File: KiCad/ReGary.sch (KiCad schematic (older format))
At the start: 10 parts, among them U3 SN74CBTD16210, U4 SN74CBTD16210, U5 SN74CBTD16210, U6 SN74CBTD16210, U7 PLCC_84_plug, U8 PLCC_84_plug

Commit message: Add Fat Gary socket symbol and change to it
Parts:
- removed U7: PLCC_84_plug, ReGary:PLCC-84_Plug_P1.27mm_mirrored, symbol ReGary:Super_Buster_socket
- added U7: PLCC_84_plug, ReGary:PLCC-84_Plug_P1.27mm_mirrored, symbol ReGary:Fat_Gary_socket
- U8: symbol ReGary:Super_Buster_socket -> ReGary:Fat_Gary_socket
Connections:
- net +5V: no longer U8.42 (VCC), U8.84 (VCC)
- net A0: no longer U8.5 (A0)
- net A1: no longer U8.4 (A1)
- net A2: no longer U8.3 (A2)
- net A3: no longer U8.48 (A3)
- net ABOE0: no longer U8.44 (~ABOE0)
- net ABOE1: no longer U8.75 (~ABOE1)
- net ABOE2: no longer U8.43 (~ABOE2)
- net ADDRZ3: no longer U8.53 (~ADDRZ3)
- net AS: no longer U8.9 (~AS)
- net BERR: no longer U8.27 (~BERR)
- net BG: no longer U8.24 (~BG)
- net BGACK: no longer U8.25 (~BGACK)
- net BIGZ: no longer U8.68 (~BIGZ)
- net BINT: no longer U8.82 (~BINT)
- net BR: no longer U8.23 (~BR)
- net C7M: no longer U8.31 (C7M)
- net CBACK: no longer U8.50 (~CBACK)
- net CBREQ: no longer U8.49 (~CBREQ)
- net CCS: no longer U8.2 (~CCS)
- net CDAC: no longer U8.32 (~CDAC)
- net CIIN: no longer U8.18 (~CIIN)
- net CINH: no longer U8.47 (~CINH)
- net CLK90: no longer U8.58 (CLK90)
- net CPUCLK: no longer U8.30 (CPUCLK)
- net D2P: no longer U8.33 (~D2P)
- net DBLT: no longer U8.37 (DBLT)
- net DBOE0: no longer U8.35 (~DBOE0)
- net DBOE1: no longer U8.34 (~DBOE1)
- net DBR16: no longer U8.36 (~DBR16)
- net DOE: no longer U8.21 (DOE)
- net DS: no longer U8.10 (~DS)
- net DSACK0: no longer U8.11 (~DSACK0)
- net DSACK1: no longer U8.12 (~DSACK1)
- net DTACK: no longer U8.20 (~DTACK)
- net EA2: no longer U8.60 (EA2)
- net EA3: no longer U8.61 (EA3)
- net EBCLR: no longer U8.63 (~EBCLR)
- net EBG0: no longer U8.74 (~EBG0)
- net EBG1: no longer U8.73 (~EBG1)
- net EBG2: no longer U8.72 (~EBG2)
- net EBG3: no longer U8.71 (~EBG3)
- net EBG4: no longer U8.69 (~EBG4)
- net EBGACK: no longer U8.57 (~EBGACK)
- net EBR0: no longer U8.80 (~EBR0)
- net EBR1: no longer U8.79 (~EBR1)
- net EBR2: no longer U8.78 (~EBR2)
- net EBR3: no longer U8.77 (~EBR3)
- net EBR4: no longer U8.76 (~EBR4)
- net EDS0: no longer U8.62 (~EDS0)
- net EDS1: no longer U8.83 (~EDS1)
- net EDS2: no longer U8.39 (~EDS2)
- net EDS3: no longer U8.40 (~EDS3)
- net FCS: no longer U8.1 (~FCS)
- net GND: no longer U8.14 (GND), U8.28 (GND), U8.56 (GND), U8.70 (GND)
- net HLT: no longer U8.26 (~HLT)
- net IOZ2: no longer U8.51 (~IOZ2)
- net LOCK_EA1: no longer U8.41 (~LOCK~/EA1)
- net MEMZ2: no longer U8.52 (MEMZ2)
- net MS0: no longer U8.81 (MS0)
- net MS1: no longer U8.54 (MS1)
- net MS2: no longer U8.45 (MS2)
- net MTACK: no longer U8.19 (~MTACK)
- net MTCR: no longer U8.46 (~MTCR)
- net OWN: no longer U8.55 (~OWN)
- net READ: no longer U8.38 (READ)
- net RESET: no longer U8.29 (~RESET)
- net RMC: no longer U8.15 (~RMC)
- net RW: no longer U8.6 (R~W)
- net SBG: no longer U8.17 (~SBG)
- net SBR: no longer U8.16 (~SBR)
- net SIZ0: no longer U8.7 (SIZ0)
- net SIZ1: no longer U8.8 (SIZ1)
- net SLAVE0: no longer U8.67 (~SLAVE0)
- net SLAVE1: no longer U8.66 (~SLAVE1)
- net SLAVE2: no longer U8.65 (~SLAVE2)
- net SLAVE3: no longer U8.64 (~SLAVE3)
- net SLAVE4: no longer U8.59 (~SLAVE4)
- net STERM: no longer U8.13 (~STERM)
- net WAIT: no longer U8.22 (~WAIT)

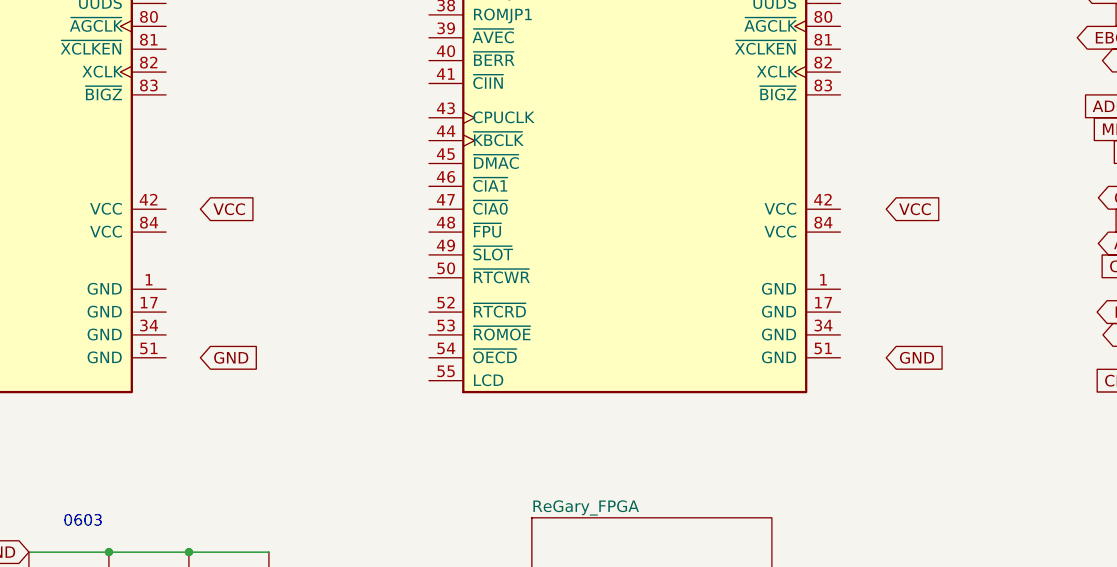
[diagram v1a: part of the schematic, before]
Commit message: Removed BGA FPGA
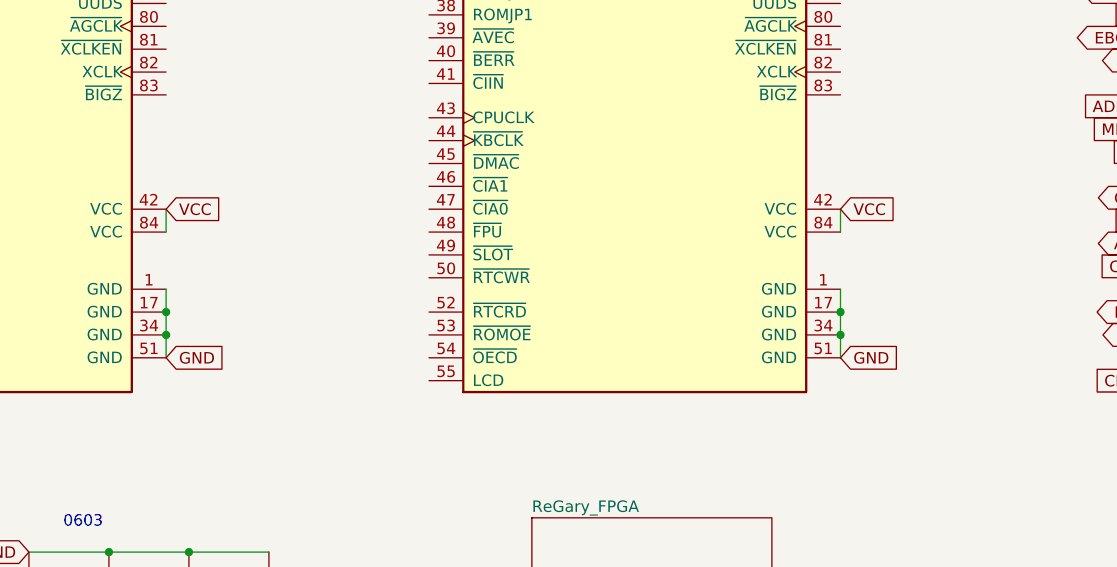
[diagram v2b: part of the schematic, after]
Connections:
- net +5V: now also U7.42 (VCC), U7.84 (VCC), U8.42 (VCC), U8.84 (VCC)
- net GND: now also U7.1 (GND), U7.17 (GND), U7.34 (GND), U7.51 (GND), U8.1 (GND), U8.17 (GND), U8.34 (GND), U8.51 (GND)
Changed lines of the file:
@@
 Text GLabel 8150 950  2    50   Input ~ 0
 GND
-Text GLabel 2900 6000 2    50   Input ~ 0
+Text GLabel 2750 6000 2    50   Input ~ 0
 GND
 Wire Wire Line
@@
 Text GLabel 8150 1250 2    50   Output ~ 0
 EBR3_FPGA
-Text GLabel 2900 5350 2    50   Input ~ 0
+Text GLabel 2750 5350 2    50   Input ~ 0
 VCC
 Text GLabel 8150 2150 2    50   BiDi ~ 0
@@
 	1    0    0    -1
 $EndComp
-Text GLabel 5900 6000 2    50   Input ~ 0
-GND
-Text GLabel 5900 5350 2    50   Input ~ 0
+Text GLabel 5700 6000 2    50   Input ~ 0
+GND
+Text GLabel 5700 5350 2    50   Input ~ 0
 VCC
 Text GLabel 9200 5100 0    50   Input ~ 0
@@
 	1    0    0    -1
 $EndComp
+Wire Wire Line
+	2750 5450 2750 5350
+Wire Wire Line
+	2750 5700 2750 5800
+Connection ~ 2750 5800
+Wire Wire Line
+	2750 5800 2750 5900
+Connection ~ 2750 5900
+Wire Wire Line
+	2750 5900 2750 6000
+Wire Wire Line
+	5700 5350 5700 5450
+Wire Wire Line
+	5700 5700 5700 5800
+Connection ~ 5700 5800
+Wire Wire Line
+	5700 5800 5700 5900
+Connection ~ 5700 5900
+Wire Wire Line
+	5700 5900 5700 6000
 $EndSCHEMATC

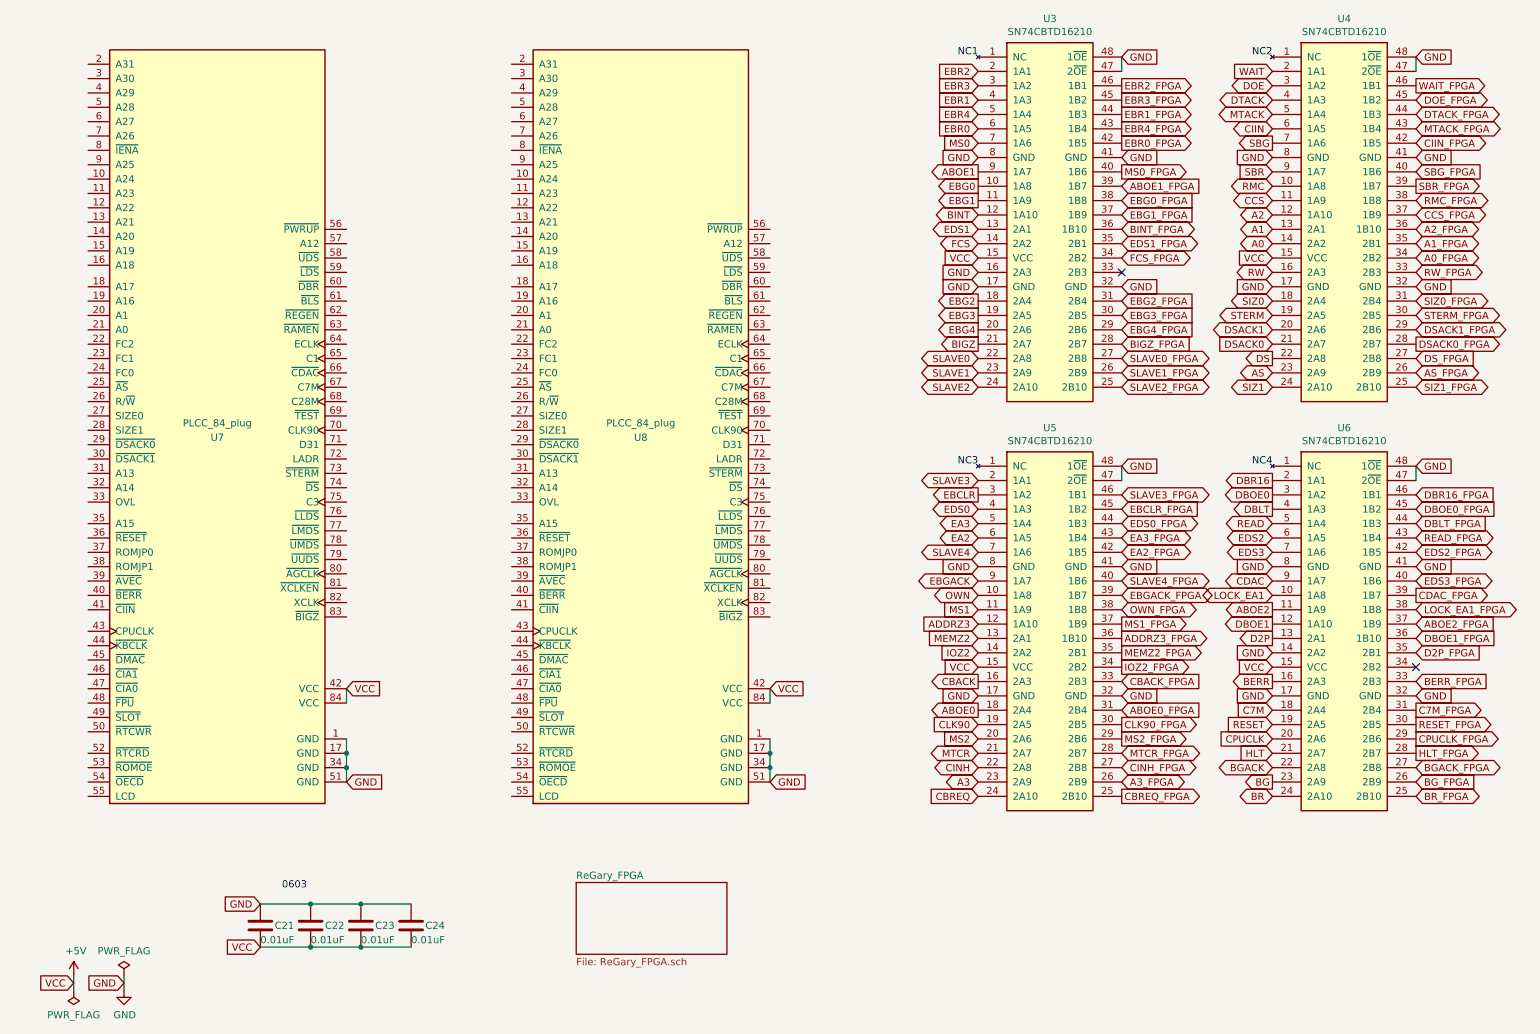
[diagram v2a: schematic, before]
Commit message: Change level shifters from CBTD to CBT with 4V3 power supply, change inner power layer from VCC to 4V3
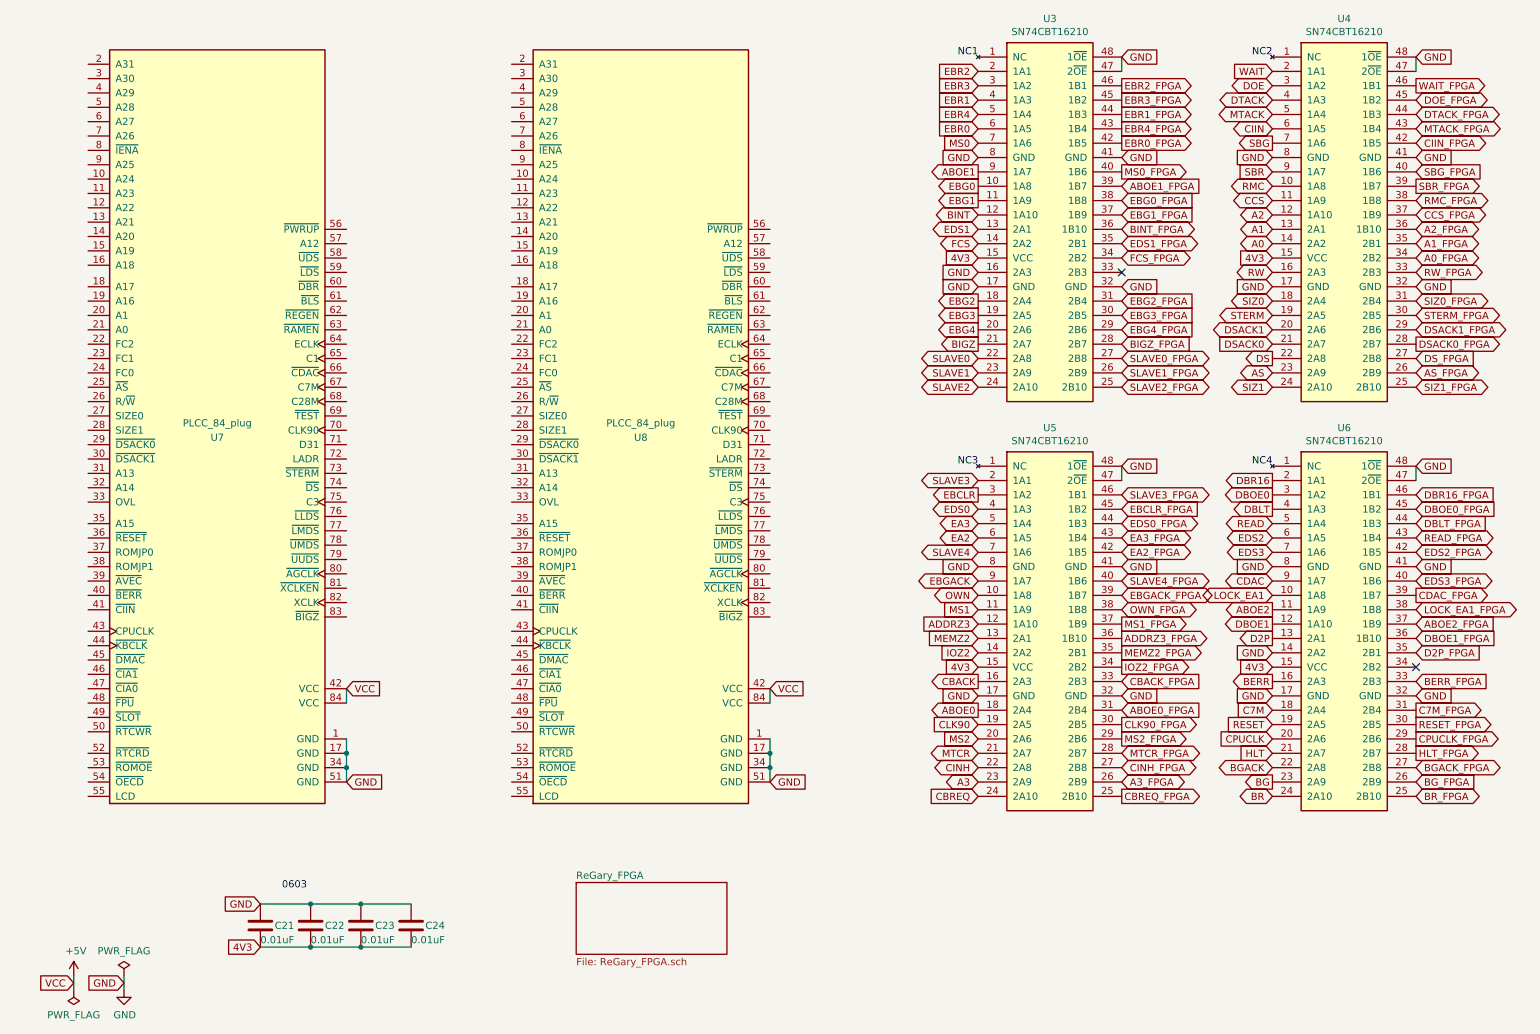
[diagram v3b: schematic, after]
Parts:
- U3, U4, U5, U6: value SN74CBTD16210 -> SN74CBT16210
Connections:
- net +5V: no longer C21.2, C22.2, C23.2, C24.2, U3.15 (VCC), U4.15 (VCC), U5.15 (VCC), U6.15 (VCC)
- new net 4V3: C21.2, C22.2, C23.2, C24.2, U3.15 (VCC), U4.15 (VCC), U5.15 (VCC), U6.15 (VCC)
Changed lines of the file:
@@
 P 9700 2050
 F 0 "U4" H 9700 3417 50  0000 C CNN
-F 1 "SN74CBTD16210" H 9700 3326 50  0000 C CNN
+F 1 "SN74CBT16210" H 9700 3326 50  0000 C CNN
 F 2 "ReGary:TSSOP-48_6.1x12.5mm_P0.5mm_padLength_1mm" H 11350 2500 50  0001 C CNN
 F 3 "https://www.ti.com/lit/ds/symlink/sn74cbtd16210.pdf" H 11350 2500 50  0001 C CNN
@@
 P 7650 4900
 F 0 "U5" H 7650 6267 50  0000 C CNN
-F 1 "SN74CBTD16210" H 7650 6176 50  0000 C CNN
+F 1 "SN74CBT16210" H 7650 6176 50  0000 C CNN
 F 2 "ReGary:TSSOP-48_6.1x12.5mm_P0.5mm_padLength_1mm" H 9300 5350 50  0001 C CNN
 F 3 "https://www.ti.com/lit/ds/symlink/sn74cbtd16210.pdf" H 9300 5350 50  0001 C CNN
@@
 P 9700 4900
 F 0 "U6" H 9700 6267 50  0000 C CNN
-F 1 "SN74CBTD16210" H 9700 6176 50  0000 C CNN
+F 1 "SN74CBT16210" H 9700 6176 50  0000 C CNN
 F 2 "ReGary:TSSOP-48_6.1x12.5mm_P0.5mm_padLength_1mm" H 11350 5350 50  0001 C CNN
 F 3 "https://www.ti.com/lit/ds/symlink/sn74cbtd16210.pdf" H 11350 5350 50  0001 C CNN
@@
 Wire Wire Line
 	2500 7150 2850 7150
-Text GLabel 7150 2350 0    50   Input ~ 0
-VCC
 Connection ~ 2850 6850
 Connection ~ 2850 7150
@@
 P 7650 2050
 F 0 "U3" H 7650 3417 50  0000 C CNN
-F 1 "SN74CBTD16210" H 7650 3326 50  0000 C CNN
+F 1 "SN74CBT16210" H 7650 3326 50  0000 C CNN
 F 2 "ReGary:TSSOP-48_6.1x12.5mm_P0.5mm_padLength_1mm" H 9300 2500 50  0001 C CNN
 F 3 "https://www.ti.com/lit/ds/symlink/sn74cbtd16210.pdf" H 9300 2500 50  0001 C CNN
@@
 Text GLabel 8150 4500 2    50   Input ~ 0
 GND
-Text GLabel 9200 2350 0    50   Input ~ 0
-VCC
 Text GLabel 9200 1650 0    50   Input ~ 0
 GND
 Text GLabel 9200 2550 0    50   Input ~ 0
 GND
-Text GLabel 9200 5200 0    50   Input ~ 0
-VCC
 Text GLabel 9200 4500 0    50   Input ~ 0
 GND
@@
 Text GLabel 7150 4500 0    50   Input ~ 0
 GND
-Text GLabel 7150 5200 0    50   Input ~ 0
-VCC
 Text GLabel 10200 3250 2    50   BiDi ~ 0
 SIZ1_FPGA
@@
 Wire Wire Line
 	2850 7150 3200 7150
-Text GLabel 2150 7150 0    50   Input ~ 0
-VCC
 Text Notes 2300 6750 0    50   ~ 0
 0603
@@
 Wire Wire Line
 	5700 5900 5700 6000
+Text GLabel 7150 2350 0    50   Input ~ 0
+4V3
+Text GLabel 9200 2350 0    50   Input ~ 0
+4V3
+Text GLabel 7150 5200 0    50   Input ~ 0
+4V3
+Text GLabel 9200 5200 0    50   Input ~ 0
+4V3
+Text GLabel 2150 7150 0    50   Input ~ 0
+4V3
 $EndSCHEMATC

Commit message: fixed placement of capacitors C8 and C9
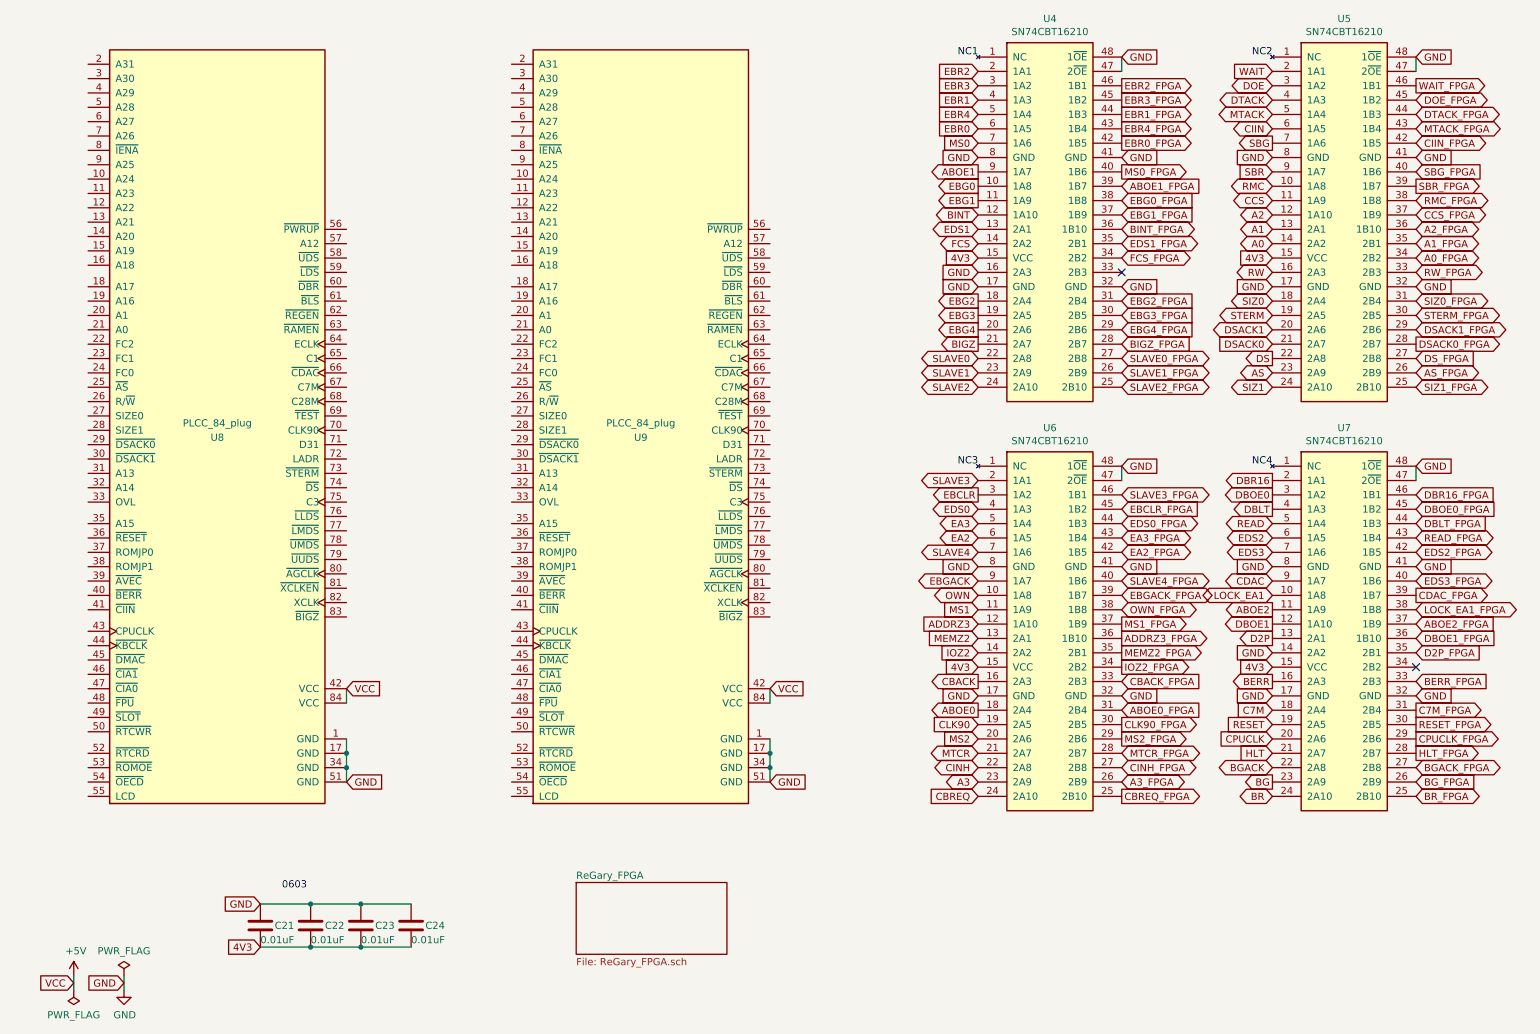
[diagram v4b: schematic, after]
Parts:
- renumbered U3 to U4, U4 to U5, U5 to U6, U6 to U7, U7 to U8, U8 to U9
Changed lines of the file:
@@
 	8150 950  8150 1050
 $Comp
-L ReGary:SN74CBTD16210 U4
+L ReGary:SN74CBTD16210 U5
 U 1 1 605AF950
 P 9700 2050
-F 0 "U4" H 9700 3417 50  0000 C CNN
+F 0 "U5" H 9700 3417 50  0000 C CNN
 F 1 "SN74CBT16210" H 9700 3326 50  0000 C CNN
 F 2 "ReGary:TSSOP-48_6.1x12.5mm_P0.5mm_padLength_1mm" H 11350 2500 50  0001 C CNN
@@
 $EndComp
 $Comp
-L ReGary:SN74CBTD16210 U5
+L ReGary:SN74CBTD16210 U6
 U 1 1 605B82D1
 P 7650 4900
-F 0 "U5" H 7650 6267 50  0000 C CNN
+F 0 "U6" H 7650 6267 50  0000 C CNN
 F 1 "SN74CBT16210" H 7650 6176 50  0000 C CNN
 F 2 "ReGary:TSSOP-48_6.1x12.5mm_P0.5mm_padLength_1mm" H 9300 5350 50  0001 C CNN
@@
 $EndComp
 $Comp
-L ReGary:SN74CBTD16210 U6
+L ReGary:SN74CBTD16210 U7
 U 1 1 605BA8E0
 P 9700 4900
-F 0 "U6" H 9700 6267 50  0000 C CNN
+F 0 "U7" H 9700 6267 50  0000 C CNN
 F 1 "SN74CBT16210" H 9700 6176 50  0000 C CNN
 F 2 "ReGary:TSSOP-48_6.1x12.5mm_P0.5mm_padLength_1mm" H 11350 5350 50  0001 C CNN
@@
 	8150 3900 8150 3800
 $Comp
-L ReGary:SN74CBTD16210 U3
+L ReGary:SN74CBTD16210 U4
 U 1 1 6058DC08
 P 7650 2050
-F 0 "U3" H 7650 3417 50  0000 C CNN
+F 0 "U4" H 7650 3417 50  0000 C CNN
 F 1 "SN74CBT16210" H 7650 3326 50  0000 C CNN
 F 2 "ReGary:TSSOP-48_6.1x12.5mm_P0.5mm_padLength_1mm" H 9300 2500 50  0001 C CNN
@@
 EDS0
 $Comp
-L ReGary:Fat_Gary_socket U8
+L ReGary:Fat_Gary_socket U9
 U 1 1 67490817
 P 4800 3500
-F 0 "U8" H 4800 3400 50  0000 C CNN
+F 0 "U9" H 4800 3400 50  0000 C CNN
 F 1 "PLCC_84_plug" H 4800 3500 50  0000 C CNN
 F 2 "ReGary:PLCC-84_TH_pin_holes" H 5200 6000 50  0001 L CIN
@@
 $EndSheet
 $Comp
-L ReGary:Fat_Gary_socket U7
+L ReGary:Fat_Gary_socket U8
 U 1 1 67BAA3CA
 P 1850 3500
-F 0 "U7" H 1850 3400 50  0000 C CNN
+F 0 "U8" H 1850 3400 50  0000 C CNN
 F 1 "PLCC_84_plug" H 1850 3500 50  0000 C CNN
 F 2 "ReGary:PLCC-84_Plug_P1.27mm_mirrored" H 2250 6000 50  0001 L CIN
